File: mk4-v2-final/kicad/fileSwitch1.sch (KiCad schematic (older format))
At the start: 2 parts

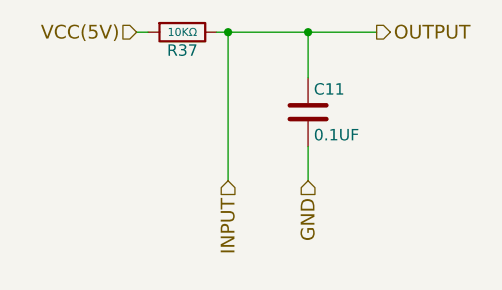
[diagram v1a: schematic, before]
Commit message: added headnight diodes, I don't think software control of them is going to be possible
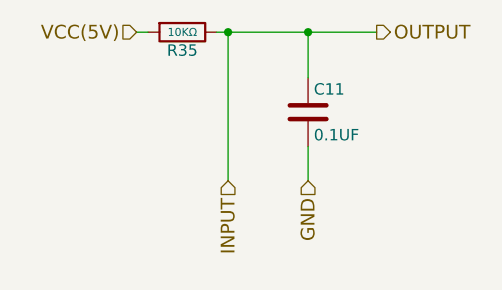
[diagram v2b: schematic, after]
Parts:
- renumbered R37 to R35
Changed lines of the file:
@@
 $EndDescr
 $Comp
-L R R37
+L R R35
 U 1 1 59DEC256
 P 5000 3550
-F 0 "R37" V 5080 3550 50  0000 C CNN
+F 0 "R35" V 5080 3550 50  0000 C CNN
 F 1 "10KΩ" V 5000 3550 35  0000 C CNN
 F 2 "Resistors_THT:R_Axial_DIN0207_L6.3mm_D2.5mm_P10.16mm_Horizontal" V 4930 3550 50  0001 C CNN

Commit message: schematic is done, footprint association and netlist are also done
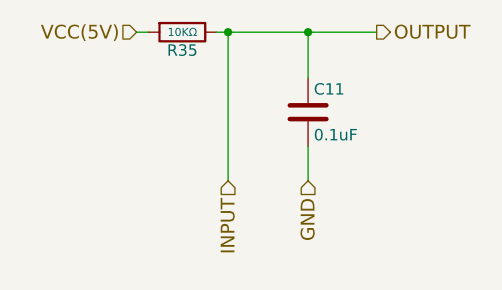
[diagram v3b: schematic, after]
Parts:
- C11: value 0.1UF -> 0.1uF; footprint Capacitors_THT:CP_Radial_D5.0mm_P2.00mm -> C_Rect_L5.08mm_W3.175mm_P2.54mm:C_Rect_L5.08mm_W3.175mm_P2.54mm; digikey-pn (none) -> 478-5096-ND; mfg-pn (none) -> AR205F104K4R
- R35: footprint Resistors_THT:R_Axial_DIN0207_L6.3mm_D2.5mm_P10.16mm_Horizontal -> Resistors_THT:R_Axial_DIN0204_L3.6mm_D1.6mm_P5.08mm_Horizontal; digikey-pn (none) -> BC10.0KXCT-ND; mfg-pn (none) -> MBA02040C1002FRP00
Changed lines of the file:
@@
 EESchema Schematic File Version 2
-LIBS:hitchco-mk4-rescue
 LIBS:power
 LIBS:device
@@
 LIBS:cd4013b
 LIBS:ncs3s1205sc
+LIBS:lca715
+LIBS:SN74HC595N
+LIBS:CD74HC4067
 LIBS:hitchco-mk4-cache
 EELAYER 25 0
@@
 $Descr USLetter 11000 8500
 encoding utf-8
-Sheet 17 54
+Sheet 14 54
 Title "sensor-mcu"
 Date "2017-10-11"
@@
 F 0 "R35" V 5080 3550 50  0000 C CNN
 F 1 "10KΩ" V 5000 3550 35  0000 C CNN
-F 2 "Resistors_THT:R_Axial_DIN0207_L6.3mm_D2.5mm_P10.16mm_Horizontal" V 4930 3550 50  0001 C CNN
+F 2 "Resistors_THT:R_Axial_DIN0204_L3.6mm_D1.6mm_P5.08mm_Horizontal" V 4930 3550 50  0001 C CNN
 F 3 "" H 5000 3550 50  0001 C CNN
+F 4 "BC10.0KXCT-ND" H 5080 3650 50  0001 C CNN "digikey-pn"
+F 5 "MBA02040C1002FRP00" H 5080 3650 50  0001 C CNN "mfg-pn"
 	1    5000 3550
 	0    1    1    0
 $EndComp
+$Comp
+L C C11
+U 1 1 5A240E99
+P 5550 3900
+F 0 "C11" H 5575 4000 50  0000 L CNN
+F 1 "0.1uF" H 5575 3800 50  0000 L CNN
+F 2 "C_Rect_L5.08mm_W3.175mm_P2.54mm:C_Rect_L5.08mm_W3.175mm_P2.54mm" H 5588 3750 50  0001 C CNN
+F 3 "http://datasheets.avx.com/AR-Series.pdf" H 5550 3900 50  0001 C CNN
+F 4 "478-5096-ND" H 5575 4100 50  0001 C CNN "digikey-pn"
+F 5 "AR205F104K4R" H 5575 4100 50  0001 C CNN "mfg-pn"
+	1    5550 3900
+	1    0    0    -1
+$EndComp
 Text HLabel 5850 3550 2    60   Output ~ 0
 OUTPUT
-Wire Wire Line
-	5550 4050 5550 4200
 Text HLabel 5550 4200 3    60   Input ~ 0
 GND
@@
 VCC(5V)
 Wire Wire Line
+	5550 4050 5550 4200
+Wire Wire Line
 	4800 3550 4850 3550
 Wire Wire Line
@@
 Wire Wire Line
 	5200 3550 5200 4200
-Connection ~ 5200 3550
 Wire Wire Line
 	5550 3750 5550 3550
+Connection ~ 5200 3550
 Connection ~ 5550 3550
-$Comp
-L C C11
-U 1 1 5A240E99
-P 5550 3900
-F 0 "C11" H 5575 4000 50  0000 L CNN
-F 1 "0.1UF" H 5575 3800 50  0000 L CNN
-F 2 "Capacitors_THT:CP_Radial_D5.0mm_P2.00mm" H 5588 3750 50  0001 C CNN
-F 3 "http://nichicon-us.com/english/products/pdfs/e-uvr.pdf" H 5550 3900 50  0001 C CNN
-	1    5550 3900
-	1    0    0    -1
-$EndComp
 $EndSCHEMATC
